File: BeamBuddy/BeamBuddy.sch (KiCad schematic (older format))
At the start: 8 parts

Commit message: Completed schematic
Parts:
- removed J?: LIM_MAX, symbol Connector_Generic:Conn_01x04
- added C? (x2): 10uF, OPL_Capacitor:C1206, symbol Device:C
- added D? (x6): GRN, symbol Device:LED
- added D? (x6): RED, symbol Device:LED
- added D?: LED_RED, OPL_Optoelectronics:LED-0603, symbol OPL_Optoelectronics:SMD-LED-CLEAR-BLUE_0603_
- added J?: EXP1, symbol Connector_Generic:Conn_02x05_Odd_Even
- added J?: EXP2, symbol Connector_Generic:Conn_02x05_Odd_Even
- added J?: Conn_01x03, symbol Connector_Generic:Conn_01x03
- added J? (x2): TEMP_DISABLE, symbol Connector_Generic:Conn_01x02
- added J?: PJ-202AH, digikey-footprints:Barrel_Jack_5.5mmODx2.1mmID_PJ-202A, symbol dk_Barrel-Power-Connectors:PJ-202A
- added J?: 12V_TERM, OPL_Connector:H2-5.0-10.5X8.0MM, symbol OPL_Connector:SCREW-TERMINAL-GREEN_2P-5.0_
- added R?: 10k, symbol Device:R
- added R?: 4.7k, symbol Device:R
- added R? (x6): 560R, symbol Device:R
- added R? (x6): 1K, symbol Device:R
- added R?: 1K, OPL_Resistor:R0603, symbol OPL_Resistor:SMD-RES-220R-5%-1_10W_0603_
- added U?: SN74AHCT14D, D14, symbol SN74AHCT14D:SN74AHCT14D
- added U?: MC7805CDTRKG, Package_TO_SOT_SMD:TO-252-2, symbol Regulator_Linear:L7805
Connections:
- net +5V: now also U?.12 (H), U?.14 (VDD), C?.1, J?.1 (Pin_1), J?.1 (Pin_1), J?.10 (Pin_10), R?.1, R?.1, R?.1, R?.1, R?.1, R?.1, R?.1, R?.2, R?.2, U?.14 (VCC), U?.3 (OUT); no longer U?.2 (D), U?.7 (VSS)
- net GND: now also U?.7 (VSS), C?.2, C?.2, D?.2 (-), J?.1, J?.2, J?.2 (Pin_2), J?.3, J?.3 (Pin_3), J?.9 (Pin_9), R?.2, R?.2, R?.2, R?.2, R?.2, R?.2, U?.2 (GND), U?.7 (GND)
- net DOOR_1: now reaches J?.1 (Pin_1), R?.2, U?.3 (C)
- net DOOR_1: now also U?.1 (1A)
- net DOOR_2: now reaches J?.3 (Pin_3), R?.2, U?.4 (B)
- net DOOR_2: now also U?.3 (2A)
- net at U?.11 (G): now also U?.1 (J)
- net LIM_X: now reaches J?.1 (Pin_1), J?.2 (Pin_2), U?.9 (E)
- net LIM_X: now also U?.13 (6A)
- net LIM_Y: now reaches J?.3 (Pin_3), J?.4 (Pin_4), U?.10 (F)
- net LIM_Y: now also U?.11 (5A)
- net FLOW: now reaches J?.1 (Pin_1), R?.2, U?.5 (A)
- net FLOW: now also U?.5 (3A)
- net CHAIN_OUT: now reaches U?.13 (K)
- net CHAIN_OUT: now also U?.9 (4A)
- new net: D?.2 (A), R?.2 (x6)
- new net: D?.1 (K), R?.1 (x6)
- new net: D?.1 (+), R?.1
- new net BEEP: J?.1 (Pin_1)
- new net ENC_A: J?.5 (Pin_5)
- new net ENC_B: J?.3 (Pin_3)
- new net ENC_SW: J?.2 (Pin_2)
- new net LASER_POT: J?.1 (Pin_1)
- new net LCD4: J?.5 (Pin_5)
- new net LCD5: J?.6 (Pin_6)
- new net LCD6: J?.7 (Pin_7)
- new net LCD7: J?.8 (Pin_8)
- new net LCD_EN: J?.3 (Pin_3)
- new net LCD_RS: J?.4 (Pin_4)
- new net RST: J?.8 (Pin_8)
- new net S_CHAIN_OUT: D?.1 (K), D?.2 (A), R?.1, U?.8 (4Y)
- new net S_DOOR_1: D?.1 (K), D?.2 (A), U?.2 (1Y)
- new net S_DOOR_2: D?.1 (K), D?.2 (A), U?.4 (2Y)
- new net S_FLOW: D?.1 (K), D?.2 (A), U?.6 (3Y)
- new net S_LIM_X: D?.1 (K), D?.2 (A), U?.12 (6Y)
- new net S_LIM_Y: D?.1 (K), D?.2 (A), U?.10 (5Y)
- new net TEMP_IN: J?.2 (Pin_2), R?.2
- new net TEMP_OUT: J?.2 (Pin_2), U?.2 (D)
- new net VIN_12V: C?.1, J?.1, J?.2, U?.1 (IN)
- no-connect marks 0 -> 9
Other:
- note added: "5V Power / 1.5A Max"
- note added: "Limits go LOW when closed\nDoor switches need pull up assume NO\nFlow Sensor NO"
- note added: "Power In 12V"
- note removed: "Limits go HIGH when closed\nDoor switches need pull up assume NO\nFlow Sensor NO"

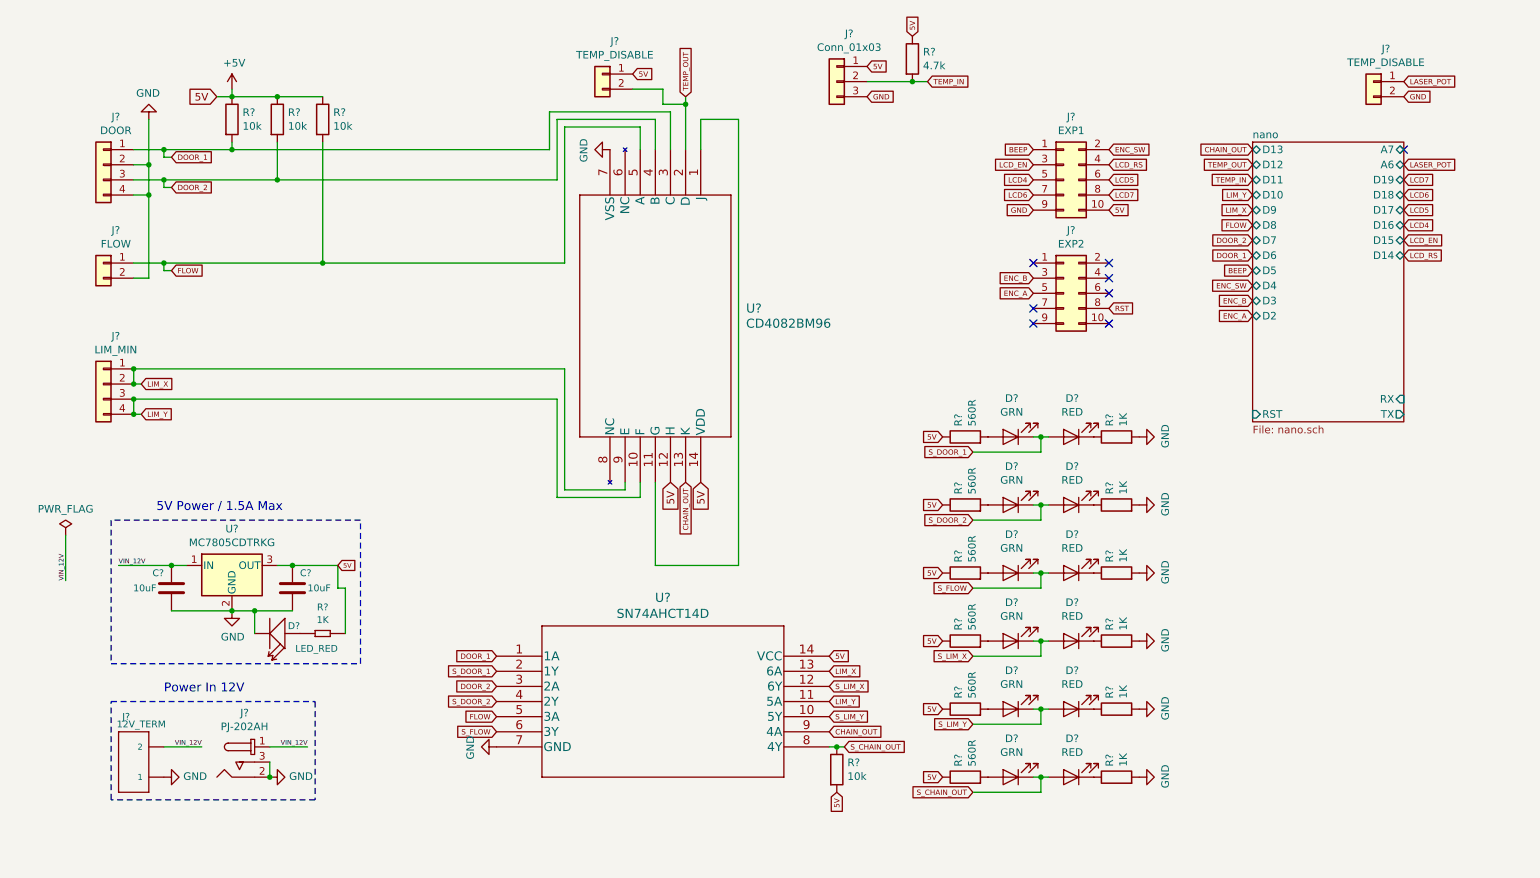
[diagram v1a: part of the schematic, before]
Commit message: Added footprints
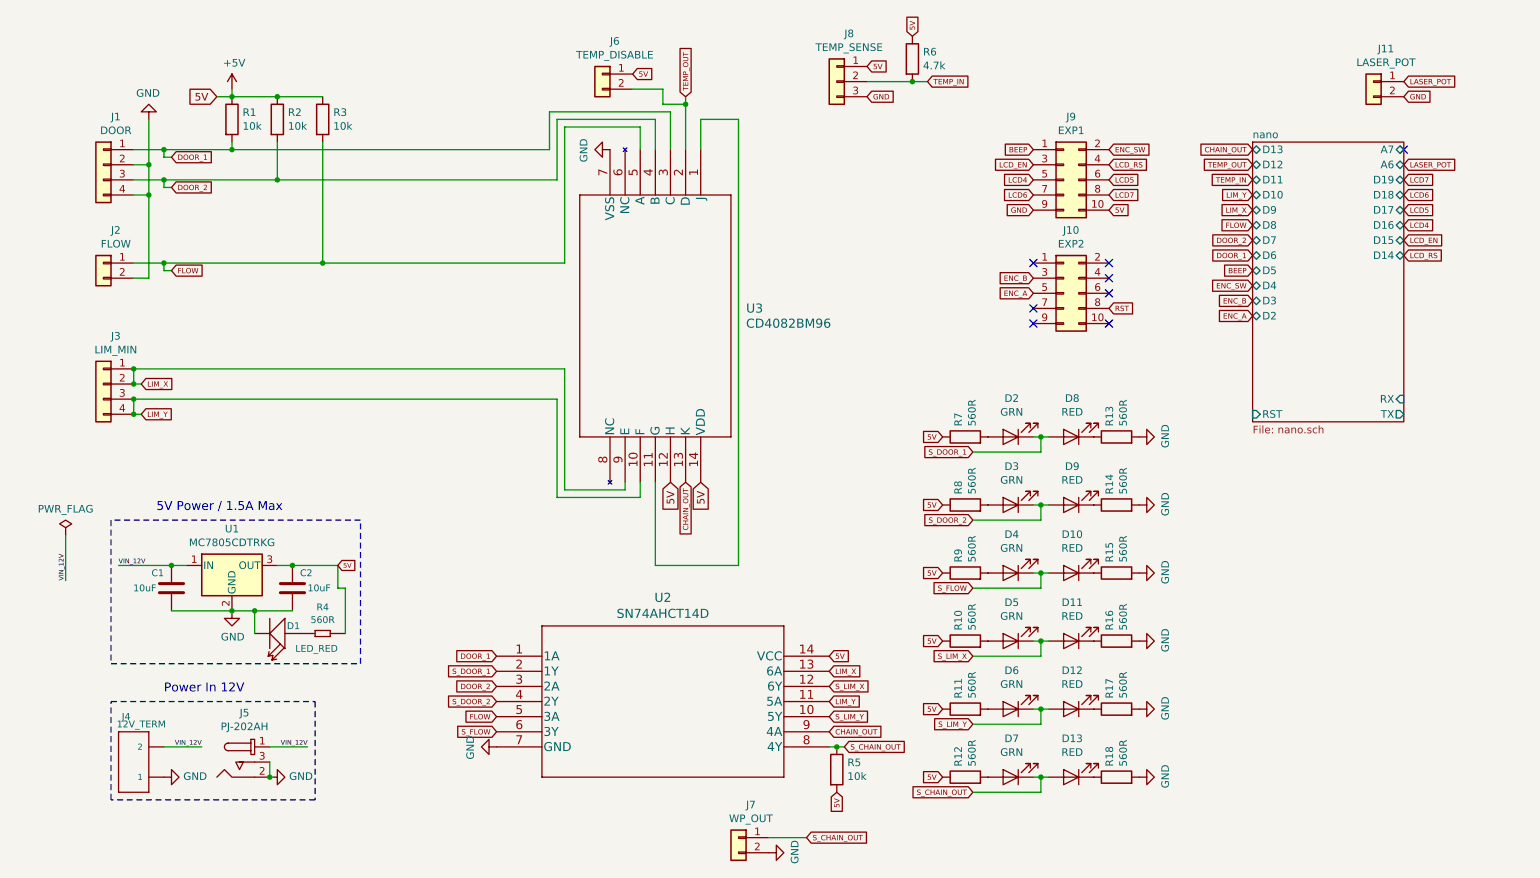
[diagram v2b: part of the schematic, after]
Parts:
- removed D? (x5): GRN, symbol Device:LED
- removed D? (x5): RED, symbol Device:LED
- removed R? (x5): 1K, symbol Device:R
- added D10, D11, D12, D13, D9: RED, LED_SMD:LED_0805_2012Metric_Castellated, symbol Device:LED
- added D3, D4, D5, D6, D7: GRN, LED_SMD:LED_0805_2012Metric_Castellated, symbol Device:LED
- added J7: WP_OUT, TerminalBlock_Phoenix:TerminalBlock_Phoenix_MPT-0,5-2-2.54_1x02_P2.54mm_Horizontal, symbol Connector_Generic:Conn_01x02
- added R14, R15, R16, R17, R18: 560R, OPL_Resistor:R0603, symbol Device:R
- D1: renamed from D?; footprint OPL_Optoelectronics:LED-0603 -> LED_SMD:LED_0805_2012Metric_Castellated; MPN 19-217-R6C-AL1M2VY-3T -> 150080VS75000; SKU 304090042 -> (none)
- D2: renamed from D?; footprint (none) -> LED_SMD:LED_0805_2012Metric_Castellated; MPN (none) -> 150080VS75000
- D8: renamed from D?; footprint (none) -> LED_SMD:LED_0805_2012Metric_Castellated; MPN (none) -> 150080RS75000
- J1, J3: renamed from J?; footprint (none) -> TerminalBlock_Phoenix:TerminalBlock_Phoenix_MPT-0,5-4-2.54_1x04_P2.54mm_Horizontal
- J10, J9: renamed from J?; footprint (none) -> Connector_IDC:IDC-Header_2x05_P2.54mm_Vertical
- J11: renamed from J?; value TEMP_DISABLE -> LASER_POT; footprint (none) -> TerminalBlock_Phoenix:TerminalBlock_Phoenix_MPT-0,5-2-2.54_1x02_P2.54mm_Horizontal
- J2: renamed from J?; footprint (none) -> TerminalBlock_Phoenix:TerminalBlock_Phoenix_MPT-0,5-2-2.54_1x02_P2.54mm_Horizontal
- J6: renamed from J?; footprint (none) -> Connector_PinHeader_2.54mm:PinHeader_1x02_P2.54mm_Vertical
- J8: renamed from J?; value Conn_01x03 -> TEMP_SENSE; footprint (none) -> TerminalBlock_Phoenix:TerminalBlock_Phoenix_MPT-0,5-3-2.54_1x03_P2.54mm_Horizontal
- R1, R10, R11, R12, R2, R3, R5, R6, R7, R8, R9: renamed from R?; footprint (none) -> OPL_Resistor:R0603
- R13: renamed from R?; value 1K -> 560R; footprint (none) -> OPL_Resistor:R0603
- R4: renamed from R?; value 1K -> 560R
- U1: renamed from U?; footprint Package_TO_SOT_SMD:TO-252-2 -> MC7805CDTRKG:MC7805CDTRKG; MPN CJ7805(TO-252-2) -> MC7805CDTRKG
- U2: renamed from U?; footprint D14 -> SN74AHCT14D:SN74AHCT14D
- U3: renamed from U?; footprint D14 -> CD4082BM96:CD4082BM96
- gave numbers to parts that had none: 4
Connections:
- net GND: now also J7.2 (Pin_2), R14.2, R15.2, R16.2, R17.2, R18.2
- net S_CHAIN_OUT: now also D13.2 (A), D7.1 (K), J7.1 (Pin_1)
- net S_DOOR_2: now also D3.1 (K), D9.2 (A)
- net S_FLOW: now also D10.2 (A), D4.1 (K)
- net S_LIM_X: now also D11.2 (A), D5.1 (K)
- net S_LIM_Y: now also D12.2 (A), D6.1 (K)
- net at R8.2: now also D3.2 (A)
- net at R9.2: now also D4.2 (A)
- net at R10.2: now also D5.2 (A)
- net at R11.2: now also D6.2 (A)
- net at R12.2: now also D7.2 (A)
- new net: D9.1 (K), R14.1
- new net: D10.1 (K), R15.1
- new net: D11.1 (K), R16.1
- new net: D12.1 (K), R17.1
- new net: D13.1 (K), R18.1

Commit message: Finished proto PCB
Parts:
- C1, C2: MPN CC1206KKX5R8BB106 -> 1276-6736-1-ND; SKU 302010181 -> 1276-6736-1-ND
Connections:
- net LIM_X: now also U2.11 (5A); no longer U2.13 (6A)
- net LIM_Y: now also U2.13 (6A); no longer U2.11 (5A)
- net S_LIM_X: now also U2.10 (5Y); no longer U2.12 (6Y)
- net S_LIM_Y: now also U2.12 (6Y); no longer U2.10 (5Y)
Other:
- note removed: "Limits go LOW when closed\nDoor switches need pull up assume NO\nFlow Sensor NO"
- note removed: "X Min\nY Min\nX Max\nY Max\nDoor 1\nDoor 2\nFlow\nTemp"
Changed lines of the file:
@@
 	-1   0    0    -1
 $EndComp
-Text Notes -1550 2400 0    118  ~ 0
-X Min\nY Min\nX Max\nY Max\nDoor 1\nDoor 2\nFlow\nTemp
 $Comp
 L Device:R R1
@@
 Wire Wire Line
 	1500 2300 1700 2300
-Text Notes -3200 3000 0    98   ~ 0
-Limits go LOW when closed\nDoor switches need pull up assume NO\nFlow Sensor NO
 $Comp
 L Connector_Generic:Conn_01x02 J2
@@
 F20 "D15" B R 9900 2150 50
 F21 "D14" B R 9900 2250 50
-F22 "TX" O R 9900 3300 50
-F23 "RX" I R 9900 3200 50
-F24 "RST" I L 8900 3300 50
+F22 "RST" I L 8900 3300 50
 $EndSheet
 NoConn ~ 11950 3800
@@
 Text GLabel 3900 5300 0    35   Input ~ 0
 FLOW
+Text GLabel 6100 5200 2    35   Input ~ 0
+LIM_X
 Text GLabel 6100 5000 2    35   Input ~ 0
-LIM_X
-Text GLabel 6100 5200 2    35   Input ~ 0
 LIM_Y
 $Comp
@@
 Text GLabel 3900 5400 0    35   Input ~ 0
 S_FLOW
+Text GLabel 6100 5300 2    35   Input ~ 0
+S_LIM_X
 Text GLabel 6100 5100 2    35   Input ~ 0
-S_LIM_X
-Text GLabel 6100 5300 2    35   Input ~ 0
 S_LIM_Y
 Text GLabel 6200 5500 2    35   Input ~ 0
@@
 F 2 "OPL_Capacitor:C1206" H 2550 4450 50  0001 C CNN
 F 3 "" H 2550 4450 50  0001 C CNN
-F 4 "CC1206KKX5R8BB106" H 2580 4600 20  0001 C CNN "MPN"
-F 5 "302010181" H 2580 4600 20  0001 C CNN "SKU"
+F 4 "1276-6736-1-ND" H 2580 4600 20  0001 C CNN "MPN"
+F 5 "1276-6736-1-ND" H 2580 4600 20  0001 C CNN "SKU"
 	1    2550 4450
 	1    0    0    -1
@@
 F 2 "OPL_Capacitor:C1206" H 1750 4450 50  0001 C CNN
 F 3 "" H 1750 4450 50  0001 C CNN
-F 4 "CC1206KKX5R8BB106" H 1780 4600 20  0001 C CNN "MPN"
-F 5 "302010181" H 1780 4600 20  0001 C CNN "SKU"
+F 4 "1276-6736-1-ND" H 1780 4600 20  0001 C CNN "MPN"
+F 5 "1276-6736-1-ND" H 1780 4600 20  0001 C CNN "SKU"
 	1    1750 4450
 	-1   0    0    -1
@@
 	0    -1   -1   0
 $EndComp
+Text GLabel 8900 3300 0    35   Input ~ 0
+RST
 $EndSCHEMATC

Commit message: Starting part value updates
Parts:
- C1: MPN 1276-6736-1-ND -> CL31A106MBHNNNE; SKU 1276-6736-1-ND -> (none); SK_PN (none) -> 1276-6736-1-ND
- C2: DK_PN (none) -> 1276-6736-1-ND; MPN 1276-6736-1-ND -> CL31A106MBHNNNE; SKU 1276-6736-1-ND -> (none)
- R4: DK_PN (none) -> 311-560HRCT-ND; MPN RC0603FR-071KL -> RC0603FR-07560RL; SKU 301010298 -> (none)
- R7, R8: DK_PN (none) -> 311-560HRCT-ND; MPN (none) -> RC0603FR-07560RL
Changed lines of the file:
@@
-$EndComp
-$Comp
-L Device:R R7
-U 1 1 5E7C381B
-P 7000 3450
-F 0 "R7" H 7070 3496 50  0000 L CNN
-F 1 "560R" H 7070 3405 50  0000 L CNN
-F 2 "OPL_Resistor:R0603" V 6930 3450 50  0001 C CNN
-F 3 "~" H 7000 3450 50  0001 C CNN
-	1    7000 3450
-	0    -1   -1   0
 $EndComp
 $Comp
@@
 F 2 "OPL_Resistor:R0603" V 6930 3900 50  0001 C CNN
 F 3 "~" H 7000 3900 50  0001 C CNN
+F 4 "311-560HRCT-ND" H 7000 3900 50  0001 C CNN "DK_PN"
+F 5 "RC0603FR-07560RL" H 7000 3900 50  0001 C CNN "MPN"
 	1    7000 3900
 	0    -1   -1   0
@@
 F 2 "OPL_Capacitor:C1206" H 2550 4450 50  0001 C CNN
 F 3 "" H 2550 4450 50  0001 C CNN
-F 4 "1276-6736-1-ND" H 2580 4600 20  0001 C CNN "MPN"
-F 5 "1276-6736-1-ND" H 2580 4600 20  0001 C CNN "SKU"
+F 4 "CL31A106MBHNNNE" H 2580 4600 20  0001 C CNN "MPN"
+F 5 "1276-6736-1-ND" H 2580 4600 20  0001 C CNN "DK_PN"
 	1    2550 4450
 	1    0    0    -1
@@
 F 2 "OPL_Capacitor:C1206" H 1750 4450 50  0001 C CNN
 F 3 "" H 1750 4450 50  0001 C CNN
-F 4 "1276-6736-1-ND" H 1780 4600 20  0001 C CNN "MPN"
-F 5 "1276-6736-1-ND" H 1780 4600 20  0001 C CNN "SKU"
+F 4 "CL31A106MBHNNNE" H 1780 4600 20  0001 C CNN "MPN"
+F 5 "1276-6736-1-ND" H 1780 4600 20  0001 C CNN "SK_PN"
 	1    1750 4450
 	-1   0    0    -1
@@
 F 2 "OPL_Resistor:R0603" H 2750 4836 40  0001 C CNN
 F 3 "" H 2750 4750 40  0001 C CNN
-F 4 "RC0603FR-071KL" H 2780 4900 20  0001 C CNN "MPN"
-F 5 "301010298" H 2780 4900 20  0001 C CNN "SKU"
+F 4 "RC0603FR-07560RL" H 2780 4900 20  0001 C CNN "MPN"
+F 5 "311-560HRCT-ND" H 2780 4900 20  0001 C CNN "DK_PN"
 	1    2750 4750
 	1    0    0    -1
@@
 Text GLabel 8900 3300 0    35   Input ~ 0
 RST
+$Comp
+L Device:R R7
+U 1 1 5E7C381B
+P 7000 3450
+F 0 "R7" H 7070 3496 50  0000 L CNN
+F 1 "560R" H 7070 3405 50  0000 L CNN
+F 2 "OPL_Resistor:R0603" V 6930 3450 50  0001 C CNN
+F 3 "~" H 7000 3450 50  0001 C CNN
+F 4 "RC0603FR-07560RL" H 7000 3450 50  0001 C CNN "MPN"
+F 5 "311-560HRCT-ND" H 7000 3450 50  0001 C CNN "DK_PN"
+	1    7000 3450
+	0    -1   -1   0
+$EndComp
 $EndSCHEMATC
